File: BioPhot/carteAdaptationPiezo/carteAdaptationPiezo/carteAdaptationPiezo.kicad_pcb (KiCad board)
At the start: 2 copper layers, 48.8 x 29.5 mm, 8 parts, among them J1 Nucleo, J2 Output, J3 POWER_IN_12V, U1 LM358

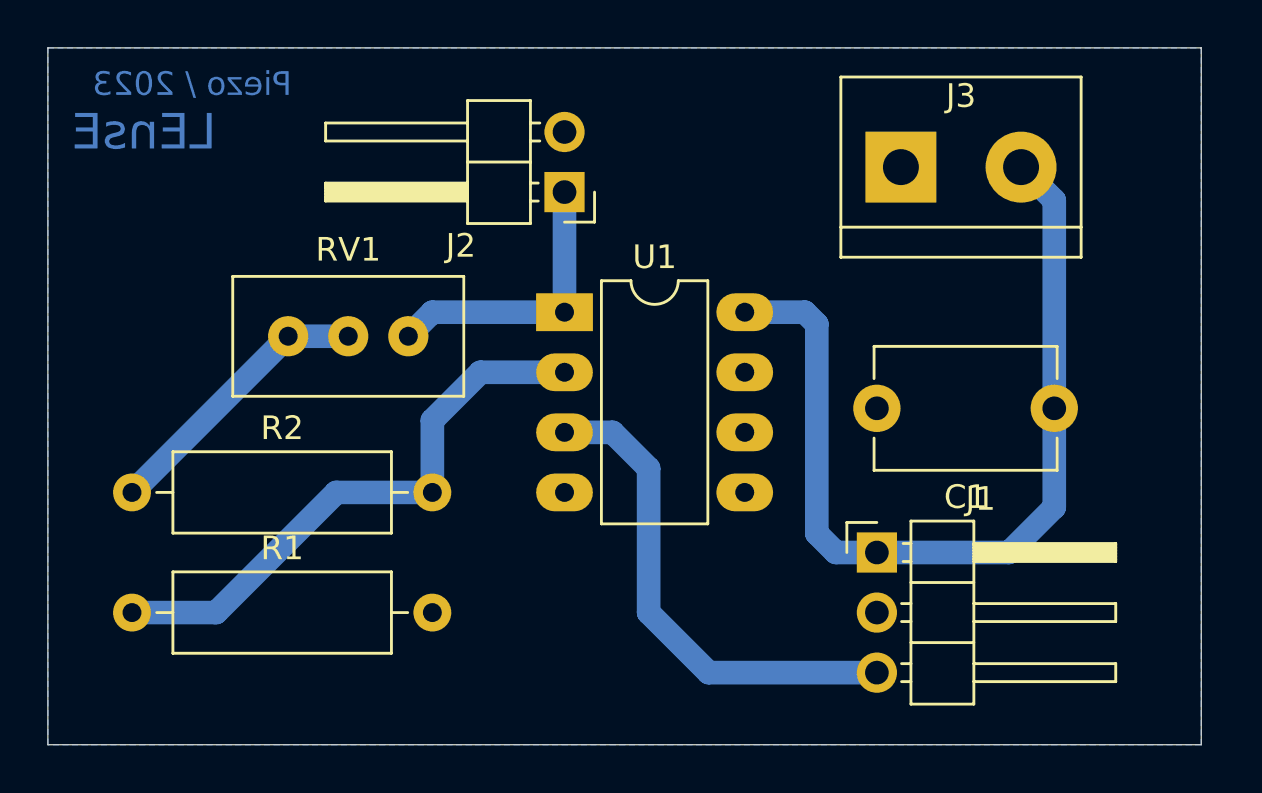
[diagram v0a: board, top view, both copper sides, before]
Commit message: Update BioPhot Interface / Schematic and PCB
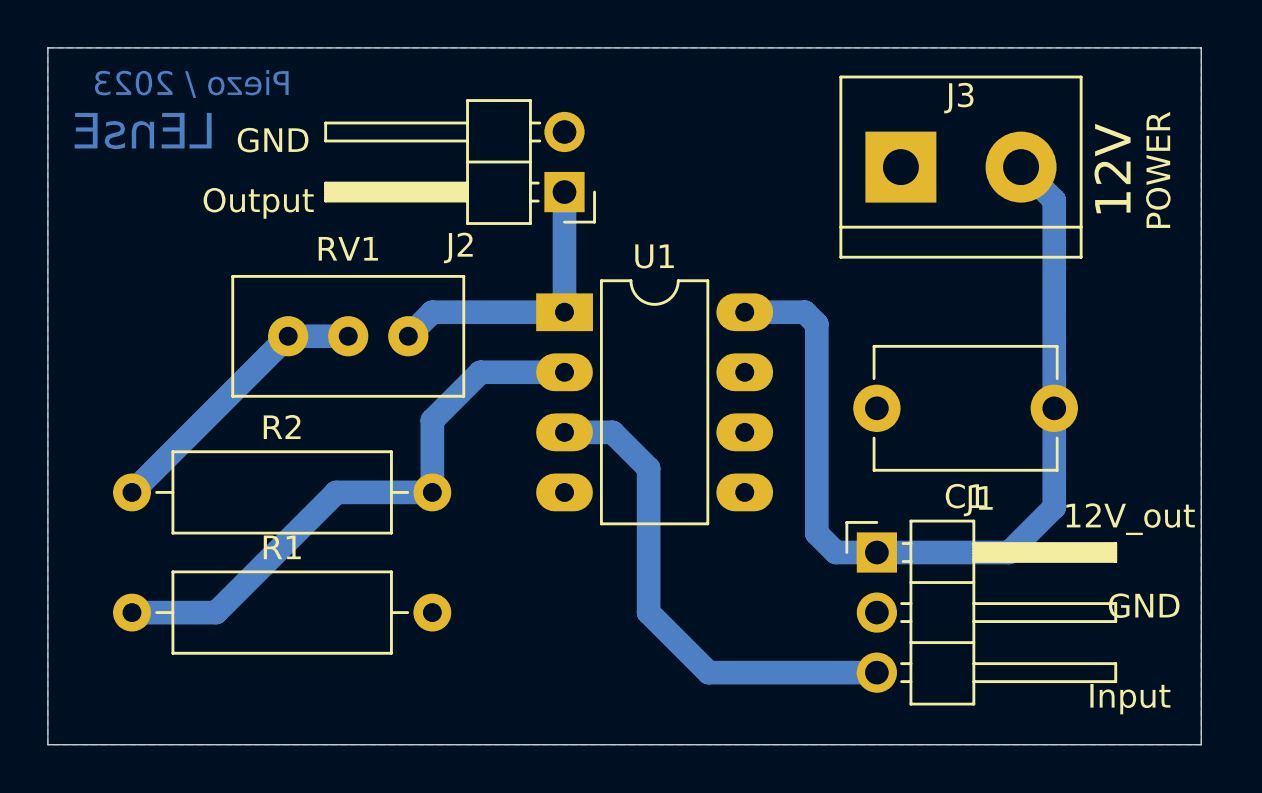
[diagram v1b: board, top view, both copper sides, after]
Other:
- board text added: "12V"
- board text added: "12V_out"
- board text added: "GND"
- board text added: "Input"
- board text added: "Output"
- board text added: "POWER"
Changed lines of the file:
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@@
-(kicad_pcb (version 20171130) (host pcbnew "(5.1.6)-1")
+(kicad_pcb (version 20171130) (host pcbnew "(5.0.1)-4")
   (general
     (thickness 1.6)
-    (drawings 6)
+    (drawings 13)
     (tracks 26)
     (zones 0)
@@
   )
   (setup
-    (last_trace_width 1)
+    (last_trace_width 0.25)
     (user_trace_width 0.8)
     (user_trace_width 1)
@@
     (zone_45_only no)
     (trace_min 0.2)
+    (segment_width 0.2)
+    (edge_width 0.05)
     (via_size 0.8)
     (via_drill 0.4)
@@
     (uvia_min_size 0.2)
     (uvia_min_drill 0.1)
-    (edge_width 0.05)
-    (segment_width 0.2)
     (pcb_text_width 0.3)
     (pcb_text_size 1.5 1.5)
@@
     (pad_drill 0.8)
     (pad_to_mask_clearance 0.05)
+    (solder_mask_min_width 0.25)
     (aux_axis_origin 0 0)
-    (visible_elements FFFFFF7F)
+    (visible_elements 7FFFFFFF)
     (pcbplotparams
       (layerselection 0x010fc_ffffffff)
@@
     )
   )
+  (gr_text 12V (at 177.165 132.715 90) (layer F.SilkS)
+    (effects (font (size 1.5 1.5) (thickness 0.3)))
+  )
+  (gr_text POWER (at 179.07 132.715 90) (layer F.SilkS)
+    (effects (font (size 1 1) (thickness 0.2)))
+  )
+  (gr_text GND (at 141.605 131.445) (layer F.SilkS)
+    (effects (font (size 1 1) (thickness 0.2)))
+  )
+  (gr_text Output (at 140.97 133.985) (layer F.SilkS)
+    (effects (font (size 1 1) (thickness 0.2)))
+  )
+  (gr_text Input (at 177.8 154.94) (layer F.SilkS)
+    (effects (font (size 1 1) (thickness 0.2)))
+  )
+  (gr_text GND (at 178.435 151.13) (layer F.SilkS)
+    (effects (font (size 1 1) (thickness 0.2)))
+  )
+  (gr_text 12V_out (at 177.8 147.32) (layer F.SilkS)
+    (effects (font (size 1 1) (thickness 0.2)))
+  )
   (gr_text LEnsE (at 136.144 131.064) (layer B.Cu)
